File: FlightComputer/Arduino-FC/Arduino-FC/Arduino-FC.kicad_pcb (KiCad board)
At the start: 2 copper layers, 95 x 86.9 mm, 30 parts, among them J1 Conn_01x04, J2 Conn_01x08, J3 Conn_01x06, J4 Conn_01x03, J5 Screw_Terminal_01x02, J6 Conn_01x02, J7 Conn_01x02, U1 NRF24L01_Breakout

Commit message: Back Silkscreen Addition
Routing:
- net GND: vias 6 -> 43
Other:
- board text added: "GitHub: https://github.com/fawaaz-kamali/CANSAT-LiteWork-2026"
- board text added: "PCB Layout By: Fawaaz Kamali Siddiqui Schematic By: Fawaaz Kamali Siddiqui Mohammad Alwattar"
- board text added: "STEC Initiative 2026 (TMU CanSat) Team 'Lite Work Fawaaz Kamali Siddiqui Hamid Karimi Mohammad Alwattar Basim Allawala Ben Reboks"

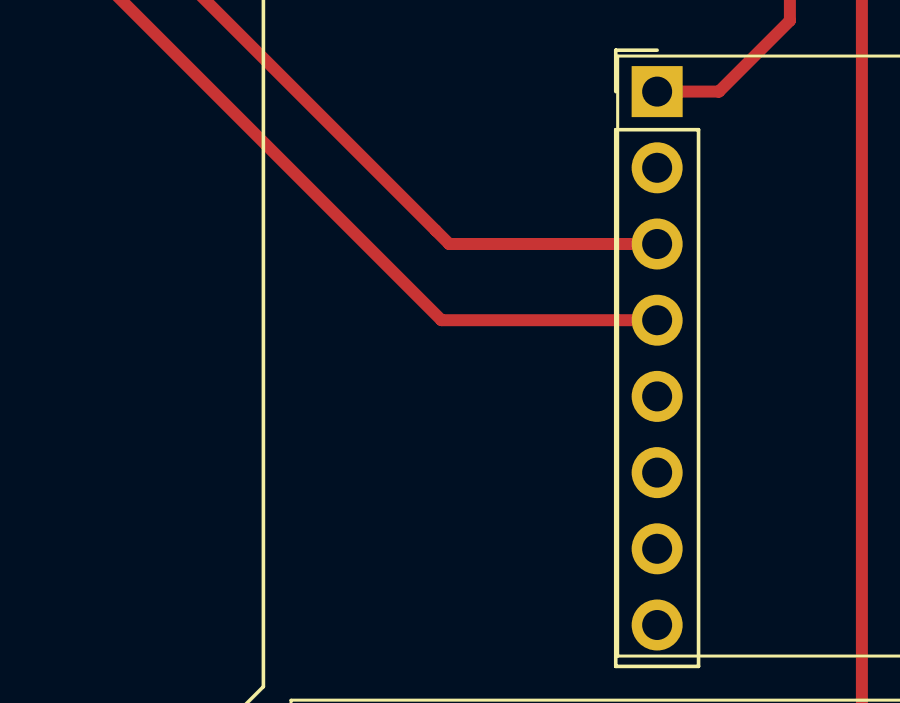
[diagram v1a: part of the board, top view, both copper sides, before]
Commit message: Added Najm Logo
- Remade production files
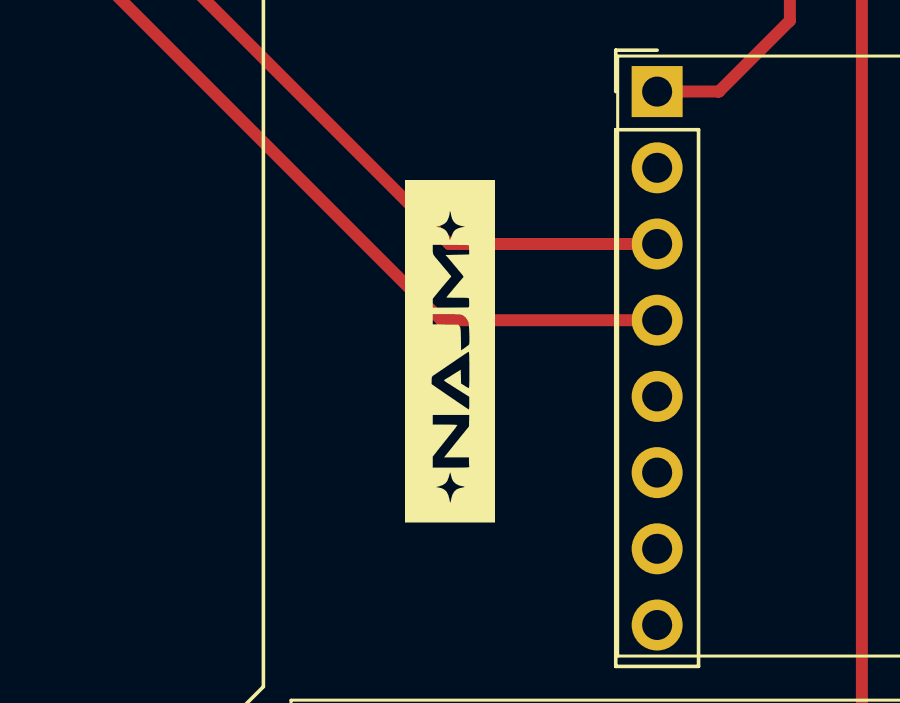
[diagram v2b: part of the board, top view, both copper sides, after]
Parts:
- added G***: LOGO, Logo:Najm_Logo, F.Cu at (179.1, 83.8)
